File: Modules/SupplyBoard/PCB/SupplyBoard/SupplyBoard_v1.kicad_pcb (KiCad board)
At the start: 2 copper layers, 46.6 x 52.4 mm, 86 parts, among them J1 CI_BATT, J2 SW-DP, J3 CIO_MAIN_CONNECTOR, Q1 AGP30P35AP, Q2 IRLM2502, SW1 RESET, SW2 SW_SPDT_312, U1 STM32L031G6Ux, U2 TPS63070, U6 TMP20AIDCK

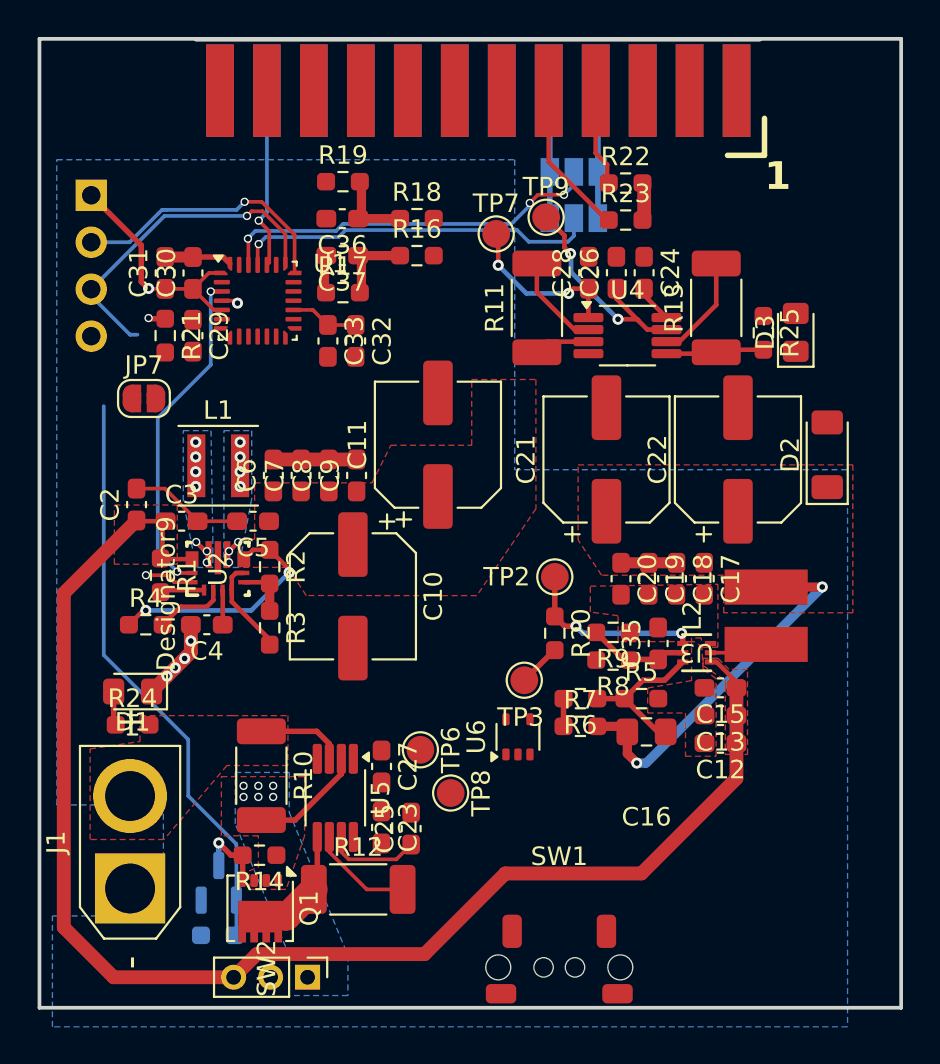
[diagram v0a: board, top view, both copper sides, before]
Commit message: Muchas cosas: Backplane, SupplyBoard y principio SensorBoard
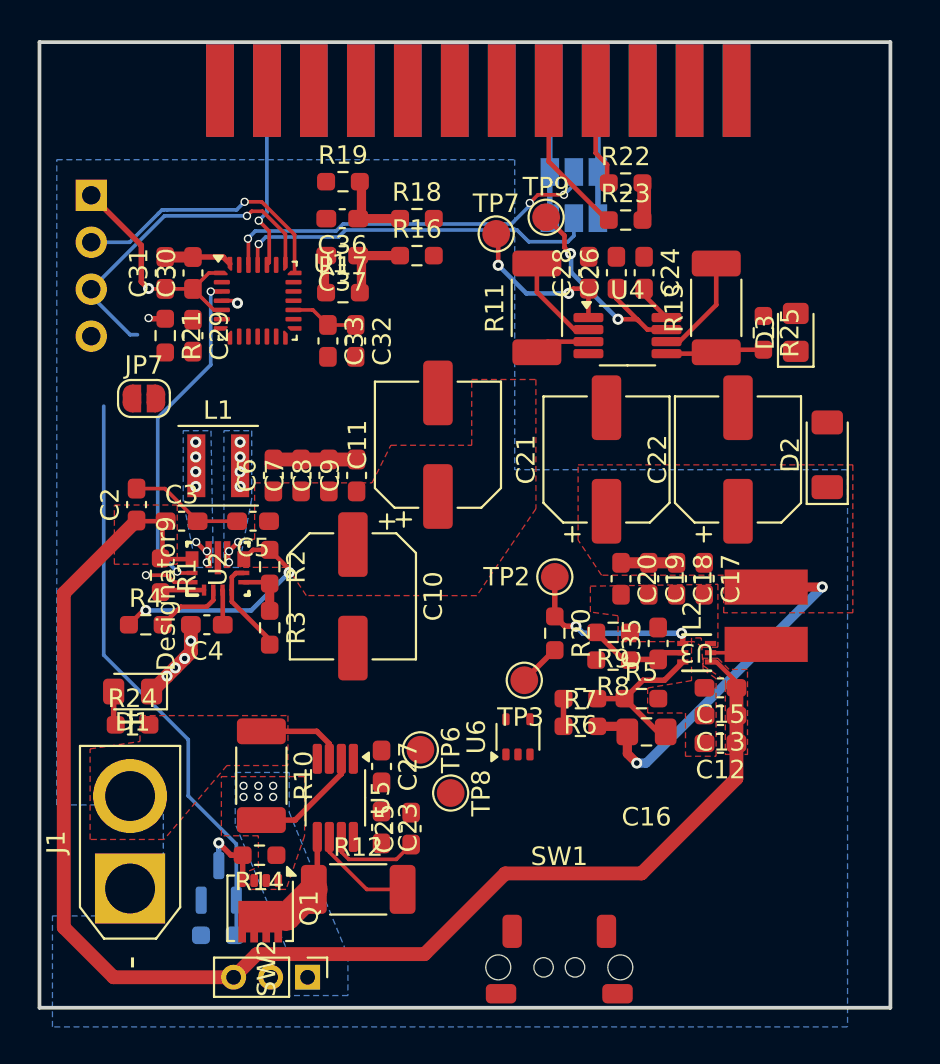
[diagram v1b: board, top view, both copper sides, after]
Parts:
- J3: moved to B.Cu
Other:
- board size 46.6 x 52.4 mm -> 46 x 52.2 mm
